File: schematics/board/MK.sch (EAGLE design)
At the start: 19 parts

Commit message: ifdhv
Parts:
- added C2, C3, C4, C5: 100nF, rcl:C-EUC0603
- added R0, R11, R12, R13, R14, R15, R16, R17, R18, R19, R22, R23, R24, R25, R7, R8: 5k1, rcl:R-US_R0603
- added R20: (no value), rcl:R-US_R2512
- added R21: (no value), rcl:R-US_0207/15
- added U$0, U$10, U$11, U$12, U$5, U$7, U$8, U$9: VT93N1, KNPN-2023:VT93N1
- added U$13, U$15: 74HC595, CanCubeSat:74HC595
- added U$14: AD5593, UNKNOWN-2024:AD5593
- added U$16: INA219AID, CanCubeSat:INA219AID
- added U$17: IRF7905PBF, UNKNOWN-2024:IRF7905PBF
- added U$18, U$19, U$20: MOLEX-2-1.25, UNKNOWN-2024:MOLEX-2-1.25
- added U$3: BOARD_SHAPE, UNKNOWN-2024:BOARD_SHAPE
- added X1, X2: JST-2-2.5, UNKNOWN-2024:JST-2-2.5
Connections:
- new net BUS+: X1.1, X2.1
- new net FOTO0: U$20.2
- new net INA_SP+: R19.1, R20.1, R21.1
- new net LATCH: U$13.STCP, U$15.STCP
- new net MOSI: U$13.DS
- new net MOTOR1+: U$13.Q4, U$18.1
- new net MOTOR1-: U$13.Q5, U$18.2
- new net MOTOR2+: U$13.Q2, U$19.1
- new net MOTOR2-: U$13.Q3, U$19.2
- new net N$10: R14.2, U$11.1, U$14.IO6
- new net N$11: C2.1, U$14.VREF
- new net N$12: R15.2, U$12.1, U$14.IO7
- new net N$15: C5.2, R19.2, U$16.A0
- new net N$16: C3.1, C4.1, U$14.VDD, U$14.VDDL
- new net N$17: R16.1, U$14.AO
- new net N$18: C5.1, R18.2, U$16.A1
- new net N$19: R17.1, U$14.RESET
- new net N$20: U$17.D2, X1.2
- new net N$21: U$17.D1, X2.2
- new net N$22: R22.1, R23.2, U$17.G2
- new net N$23: R24.1, R25.2, U$17.G1
- new net N$35: U$13.Q7S, U$15.DS
- new net N$4: R0.2, U$0.1, U$14.IO0
- new net N$5: R8.2, U$14.IO2, U$7.1
- new net N$6: R7.2, U$14.IO1, U$5.1
- new net N$7: R11.2, U$14.IO3, U$8.1
- new net N$8: R12.2, U$14.IO4, U$9.1
- new net N$9: R13.2, U$10.1, U$14.IO5
- new net PERE1: R23.1, U$13.Q6
- new net PERE2: R25.1, U$13.Q7
- new net SCK: U$13.SHCP, U$15.SHCP
- new net SHIFT3: U$15.Q7S
- new net SP+: R18.1, R20.2
- new net SP-: R21.2
- net 3V3: now also R0.1, R11.1, R12.1, R13.1, R14.1, R15.1, R17.2, R7.1, R8.1, U$13.MR, U$13.VCC, U$15.MR, U$15.VCC, U$16.SCL
- net BUZZER: now also U$13.Q1
- net GND: now also C2.2, C3.2, C4.2, R16.2, R22.2, R24.2, U$0.2, U$10.2, U$11.2, U$12.2, U$13.GND, U$13.OE, U$14.GND, U$15.GND, U$15.OE, U$16.IN+, U$16.IN-, U$16.SDA, U$17.S1, U$17.S2, U$20.1, U$5.2, U$7.2, U$8.2, U$9.2
- net SCL: now also U$14.SCL, U$16.VS
- net SDA: now also U$14.SDA, U$16.GND

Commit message: пам пам тидам
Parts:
- added R26, R27, R28, R29, R30, R31, R32, R33, R34, R35, R36, R37: 5k1, rcl:R-US_R0603
- added U$21: MOSFET_2P+2N_AP9930GM, UNKNOWN-2024:MOSFET_2P+2N_AP9930GM
- added U$22, U$23: NDC7002N, UNKNOWN-2024:NDC7002N
- U$15: value 74HC595 -> MOSFET_2P+2N_AP9930GM; device CanCubeSat:74HC595 -> UNKNOWN-2024:MOSFET_2P+2N_AP9930GM
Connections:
- removed net SHIFT3: U$15.Q7S
- new net MK_MOTOR1+: R37.1
- new net MK_MOTOR1-: R36.1
- new net MK_MOTOR2+: R31.1
- new net MK_MOTOR2-: R30.1
- new net N$24: R32.2, R34.1, U$21.N1G, U$21.P1G, U$23.D1
- new net N$25: R26.2, R28.1, U$15.N1G, U$15.P1G, U$22.D1
- new net N$26: R27.2, R29.1, U$15.N2G, U$15.P2G, U$22.D2
- new net N$27: R33.2, R35.1, U$21.N2G, U$21.P2G, U$23.D2
- new net N$28: R34.2, R36.2, U$23.G1
- new net N$29: R35.2, R37.2, U$23.G2
- new net N$32: R28.2, R30.2, U$22.G1
- new net SHIFT2: U$13.Q7S
- net 3V3: no longer U$15.MR, U$15.VCC
- net 5V: now also R26.1, R27.1, R32.1, R33.1, U$15.P1P2S, U$21.P1P2S
- net GND: now also U$15.N1N2S, U$21.N1N2S, U$22.S1, U$22.S2, U$23.S1, U$23.S2; no longer U$15.GND, U$15.OE
- net LATCH: no longer U$15.STCP
- net MOTOR1+: now also U$21.P2N2D
- net MOTOR1-: now also U$21.P1N1D
- net MOTOR2+: now also U$15.P2N2D
- net MOTOR2-: now also U$15.P1N1D
- net N$35: now also R29.2, R31.2, U$22.G2; no longer U$13.Q7S, U$15.DS
- net SCK: no longer U$15.SHCP

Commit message: Платки там
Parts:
- removed R15: 5k1, rcl:R-US_R0603
- removed U$10, U$11, U$12, U$5, U$7, U$8, U$9: VT93N1, KNPN-2023:VT93N1
- added JP1: (no value), pinhead:PINHD-1X10
- added JP2: (no value), pinhead:PINHD-1X16
- added R39, R40, R41, R42, R43, R44, R45, R46: 5k1, rcl:R-US_R0603
- R20: value (none) -> R05
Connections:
- net SD_CK renamed CK_SD
- removed net N$10: R14.2, U$11.1, U$14.IO6
- removed net N$12: R15.2, U$12.1, U$14.IO7
- removed net N$5: R8.2, U$14.IO2, U$7.1
- new net CO: R8.2, U$14.IO2
- new net CS_LIS: STM.PA10
- new net CS_LSM: STM.PA9
- new net H3: R12.2, U$14.IO4
- new net M0_RADIO: STM.PB1
- new net M1_RADIO: STM.PB10
- new net MICS: R13.2, U$14.IO5
- new net MISO_SENS: STM.PB4
- new net MOSI_SENS: STM.PB5
- new net N$34: R13.1, R45.2
- new net N$36: R12.1, R43.2
- new net N$37: R11.1, R41.2
- new net NO2: R11.2, U$14.IO3
- new net RX_GPS: STM.PA3
- new net RX_LIDAR: STM.PA12
- new net RX_RADIO: STM.PB3
- new net SCK_SENS: STM.PA5
- new net TX_GPS: STM.PA2
- new net TX_LIDAR: STM.PA11
- new net TX_RADIO: STM.PA15
- net 3V3: now also R40.1, R42.1, R44.1, R46.1; no longer R11.1, R12.1, R13.1, R14.1, R15.1, R8.1
- net 5V: now also R39.2, R8.1
- net ADC_FOTO: no longer STM.PA0
- net CE_RADIO: no longer STM.PC13
- net CS_RADIO: no longer STM.PC14
- net DIR_DRIVER: no longer STM.PA10
- net FOTO0: now also R7.2, U$14.IO1
- net GND: now also R14.1; no longer U$10.2, U$11.2, U$12.2, U$13.OE, U$5.2, U$7.2, U$8.2, U$9.2
- net IRQ_RADIO: no longer STM.PC15
- net MISO_RADIO: no longer STM.PA11
- net MISO_SR: no longer STM.PB4
- net MOSI_RADIO: no longer STM.PA1
- net MOSI_SR: no longer STM.PB5
- net N$6: now also R39.1, R40.2; no longer R7.2, U$14.IO1, U$5.1
- net N$7: now also R41.1, R42.2; no longer R11.2, U$14.IO3, U$8.1
- net N$8: now also R43.1, R44.2; no longer R12.2, U$14.IO4, U$9.1
- net N$9: now also R45.1, R46.2; no longer R13.2, U$10.1, U$14.IO5
- net OE_SR: now also R14.2, U$13.OE
- net RX1_BLE: no longer STM.PB3
- net RX2_GPS: no longer STM.PA3
- net SCK_RADIO: no longer STM.PB13
- net SCK_SR: no longer STM.PA5
- net STEP_DRIVER: no longer STM.PA9
- net SW_AMP: no longer STM.PA4
- net TX1_BLE: no longer STM.PA15
- net TX2_GPS: no longer STM.PA2
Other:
- moved on the sheet: BME280, BUZZER, C1, C2, C3, C4, C5, MICRO_SD, R0, R1, R10, R11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

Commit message: ПЛАТЫ, АААААААААААААААААААААААААААА
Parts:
- JP2: device pinhead:PINHD-1X16 -> pinhead:PINHD-1X18
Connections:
- removed net BUS+: X1.1, X2.1
- new net 4V: JP1.10, X1.1, X2.1
- new net AUX_RADIO: JP2.10, STM.PC13
- new net C0: JP2.1
- new net GERMO: JP2.18, U$13.Q0
- new net NH3: JP2.3
- new net OE: JP1.4
- new net SHIFT_2: JP2.17
- net 3V3: now also JP2.6
- net 5V: now also JP2.7
- net BUZZER: no longer STM.PB0
- net CS_LIS: now also JP1.8
- net CS_LSM: now also JP1.9
- net GND: now also JP2.5
- net LATCH: now also JP1.5
- net M0_RADIO: now also JP2.12, STM.PC15; no longer STM.PB1
- net M1_RADIO: now also JP2.11, STM.PC14; no longer STM.PB10
- net MICS: now also JP2.4
- net MISO_SENS: now also JP1.2
- net MOSI_SENS: now also JP1.1
- net NO2: now also JP2.2
- net RX_GPS: now also JP2.14
- net RX_LIDAR: now also JP2.15
- net RX_RADIO: now also JP1.6
- net SCK_SENS: now also JP1.3
- net SCL: now also JP2.9
- net SDA: now also JP2.8
- net TX_GPS: now also JP2.13
- net TX_LIDAR: now also JP2.16
- net TX_RADIO: now also JP1.7
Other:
- moved on the sheet: JP1, U$4, U$6

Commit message: схемы плат
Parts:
- removed R11, R12, R13, R39, R40, R41, R42, R43, R44, R45, R46, R8: 5k1, rcl:R-US_R0603
- R0, R7: value 5k1 -> 2k2
- renumbered STM to STM32F411, U$18 to MOTOR_SP_V, U$19 to MOTOR_SP_G, U$20 to FOTO0, X1 to PERE1, X2 to PERE2
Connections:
- removed net H3: R12.2, U$14.IO4
- removed net N$34: R13.1, R45.2
- removed net N$36: R12.1, R43.2
- removed net N$37: R11.1, R41.2
- removed net N$6: R39.1, R40.2
- removed net N$7: R41.1, R42.2
- removed net N$8: R43.1, R44.2
- removed net N$9: R45.1, R46.2
- net 3V3: no longer R40.1, R42.1, R44.1, R46.1
- net 5V: no longer R39.2, R8.1
- net CO: no longer R8.2
- net MICS: no longer R13.2
- net NH3: now also U$14.IO4
- net NO2: no longer R11.2
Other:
- moved on the sheet: C1, R5, R6

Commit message: подготовлены файлы для зимней сессии
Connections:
- removed net LATCH: JP1.5, U$13.STCP
- removed net OE: JP1.4
- removed net SHIFT2: U$13.Q7S
- removed net SHIFT_2: JP2.17
- new net SHIFT: JP2.17, U$13.Q7S
- net LATCH_SR: now also JP1.5, U$13.STCP
- net OE_SR: now also JP1.4
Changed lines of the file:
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@@
 <sheet>
 <plain>
+<wire x1="-208.28" y1="154.94" x2="327.66" y2="154.94" width="0.1524" layer="90"/>
+<wire x1="327.66" y1="154.94" x2="327.66" y2="-109.22" width="0.1524" layer="90"/>
+<wire x1="327.66" y1="-109.22" x2="-208.28" y2="-109.22" width="0.1524" layer="90"/>
+<wire x1="-208.28" y1="-109.22" x2="-208.28" y2="154.94" width="0.1524" layer="90"/>
 </plain>
 <instances>
@@
 <pinref part="R14" gate="G$1" pin="2"/>
 </segment>
+<segment>
+<wire x1="-160.02" y1="88.9" x2="-193.04" y2="88.9" width="0.1524" layer="91"/>
+<label x="-193.04" y="88.9" size="1.778" layer="95"/>
+<pinref part="JP1" gate="A" pin="4"/>
+</segment>
 </net>
 <net name="LATCH_SR" class="0">
@@
 <label x="-355.6" y="-81.28" size="1.778" layer="95"/>
 <pinref part="U$4" gate="G$1" pin="9"/>
+</segment>
+<segment>
+<wire x1="-160.02" y1="86.36" x2="-193.04" y2="86.36" width="0.1524" layer="91"/>
+<label x="-193.04" y="86.36" size="1.778" layer="95"/>
+<pinref part="JP1" gate="A" pin="5"/>
+</segment>
+<segment>
+<pinref part="U$13" gate="G$1" pin="STCP"/>
+<wire x1="93.98" y1="81.28" x2="104.14" y2="81.28" width="0.1524" layer="91"/>
+<label x="96.52" y="81.28" size="1.778" layer="95"/>
 </segment>
 </net>
@@
 </segment>
 </net>
-<net name="LATCH" class="0">
-<segment>
-<pinref part="U$13" gate="G$1" pin="STCP"/>
-<wire x1="93.98" y1="81.28" x2="104.14" y2="81.28" width="0.1524" layer="91"/>
-<label x="96.52" y="81.28" size="1.778" layer="95"/>
-</segment>
-<segment>
-<wire x1="-160.02" y1="86.36" x2="-193.04" y2="86.36" width="0.1524" layer="91"/>
-<label x="-193.04" y="86.36" size="1.778" layer="95"/>
-<pinref part="JP1" gate="A" pin="5"/>
-</segment>
-</net>
 <net name="MOTOR2+" class="0">
 <segment>
@@
 </segment>
 </net>
-<net name="SHIFT2" class="0">
+<net name="SHIFT" class="0">
 <segment>
 <pinref part="U$13" gate="G$1" pin="Q7S"/>
 <wire x1="93.98" y1="73.66" x2="104.14" y2="73.66" width="0.1524" layer="91"/>
 <label x="96.52" y="73.66" size="1.778" layer="95"/>
+</segment>
+<segment>
+<wire x1="-193.04" y1="17.78" x2="-160.02" y2="17.78" width="0.1524" layer="91"/>
+<label x="-193.04" y="17.78" size="1.778" layer="95"/>
+<pinref part="JP2" gate="A" pin="17"/>
 </segment>
 </net>
@@
 </segment>
 </net>
-<net name="OE" class="0">
-<segment>
-<wire x1="-160.02" y1="88.9" x2="-193.04" y2="88.9" width="0.1524" layer="91"/>
-<label x="-193.04" y="88.9" size="1.778" layer="95"/>
-<pinref part="JP1" gate="A" pin="4"/>
-</segment>
-</net>
 <net name="4V" class="0">
 <segment>
@@
 </segment>
 </net>
-<net name="SHIFT_2" class="0">
-<segment>
-<wire x1="-193.04" y1="17.78" x2="-160.02" y2="17.78" width="0.1524" layer="91"/>
-<label x="-193.04" y="17.78" size="1.778" layer="95"/>
-<pinref part="JP2" gate="A" pin="17"/>
-</segment>
-</net>

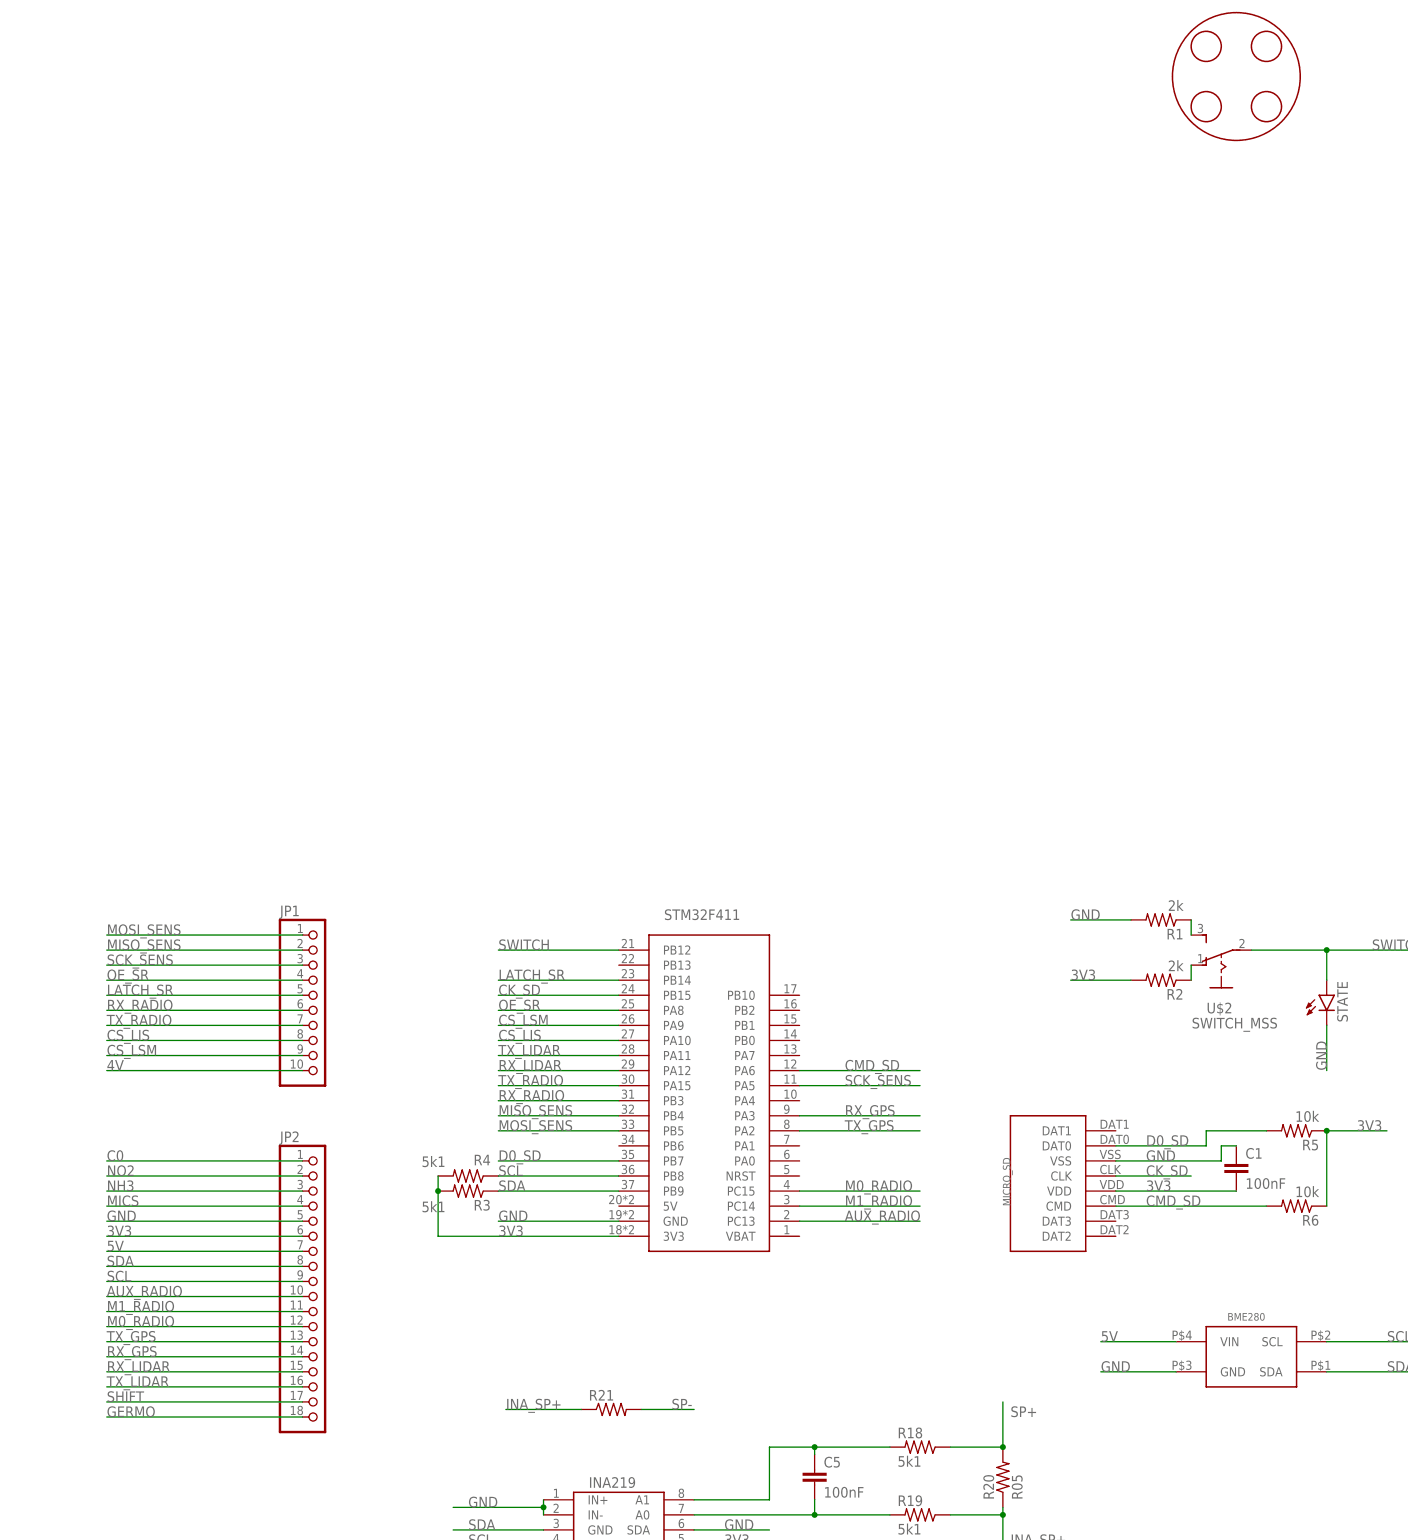
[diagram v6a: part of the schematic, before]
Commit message: распиновка разъемов плат
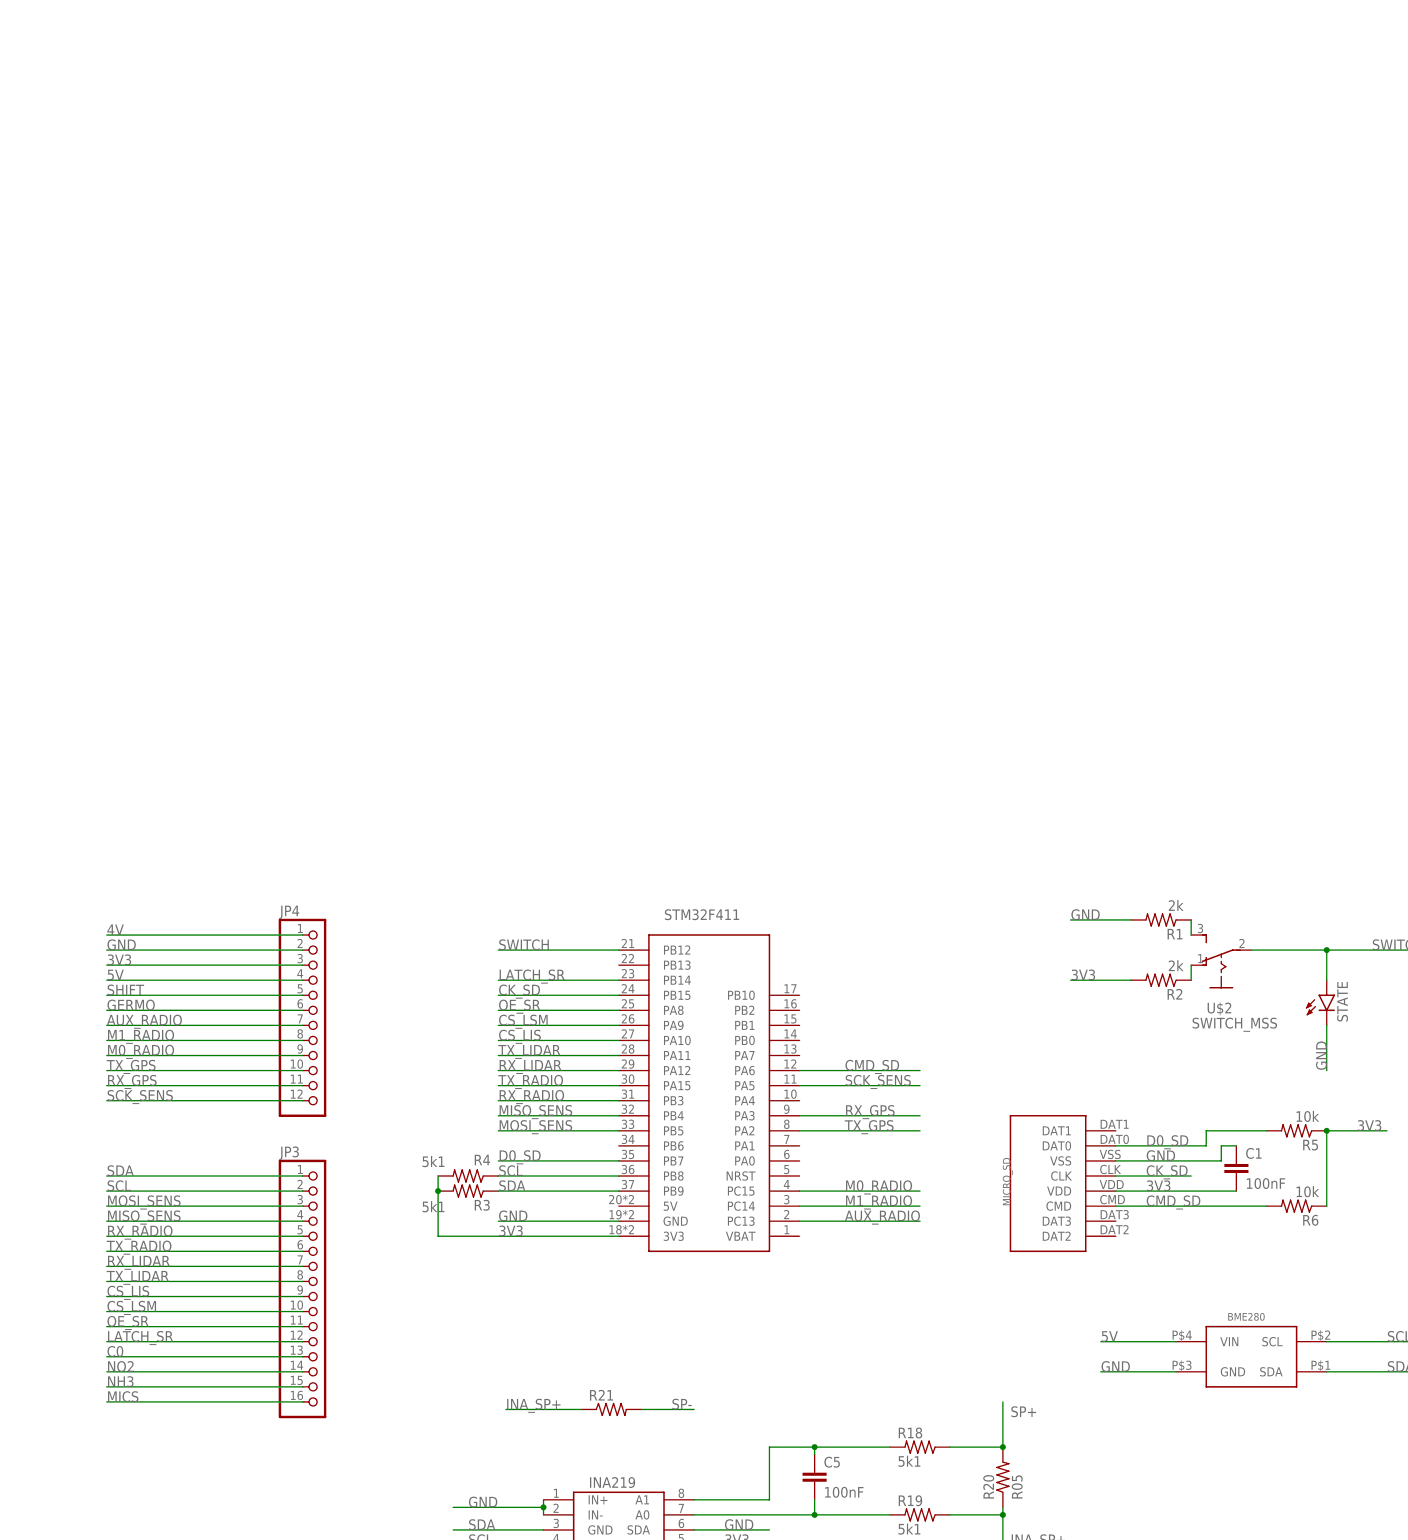
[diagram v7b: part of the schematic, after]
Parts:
- removed JP1: (no value), pinhead:PINHD-1X10
- removed JP2: (no value), pinhead:PINHD-1X18
- removed U$3: BOARD_SHAPE, UNKNOWN-2024:BOARD_SHAPE
- added JP3: (no value), pinhead:PINHD-1X16
- added JP4: (no value), pinhead:PINHD-1X12
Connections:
- net 3V3: now also JP4.3; no longer JP2.6
- net 4V: now also JP4.1; no longer JP1.10
- net 5V: now also JP4.4; no longer JP2.7
- net AUX_RADIO: now also JP4.7; no longer JP2.10
- net C0: now also JP3.13; no longer JP2.1
- net CS_LIS: now also JP3.9; no longer JP1.8
- net CS_LSM: now also JP3.10; no longer JP1.9
- net GERMO: now also JP4.6; no longer JP2.18
- net GND: now also JP4.2; no longer JP2.5
- net LATCH_SR: now also JP3.12; no longer JP1.5
- net M0_RADIO: now also JP4.9; no longer JP2.12
- net M1_RADIO: now also JP4.8; no longer JP2.11
- net MICS: now also JP3.16; no longer JP2.4
- net MISO_SENS: now also JP3.4; no longer JP1.2
- net MOSI_SENS: now also JP3.3; no longer JP1.1
- net NH3: now also JP3.15; no longer JP2.3
- net NO2: now also JP3.14; no longer JP2.2
- net OE_SR: now also JP3.11; no longer JP1.4
- net RX_GPS: now also JP4.11; no longer JP2.14
- net RX_LIDAR: now also JP3.7; no longer JP2.15
- net RX_RADIO: now also JP3.5; no longer JP1.6
- net SCK_SENS: now also JP4.12; no longer JP1.3
- net SCL: now also JP3.2; no longer JP2.9
- net SDA: now also JP3.1; no longer JP2.8
- net SHIFT: now also JP4.5; no longer JP2.17
- net TX_GPS: now also JP4.10; no longer JP2.13
- net TX_LIDAR: now also JP3.8; no longer JP2.16
- net TX_RADIO: now also JP3.6; no longer JP1.7

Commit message: jhgh
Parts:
- removed U$4: PBS_SMD_X13, UNKNOWN-2024:PBS_SMD_X13
- removed U$6: PBS_SMD_X9, UNKNOWN-2024:PBS_SMD_X9
- added SP: MOLEX-2-1.25, UNKNOWN-2024:MOLEX-2-1.25
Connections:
- removed net ADC_FOTO: U$4.4
- removed net CE_RADIO: U$6.9
- removed net CS_RADIO: U$6.8
- removed net DIR_DRIVER: U$4.12
- removed net IRQ_RADIO: U$6.7
- removed net MISO_RADIO: U$6.5
- removed net MISO_SR: U$4.6
- removed net MOSI: U$13.DS
- removed net MOSI_RADIO: U$6.6
- removed net MOSI_SR: U$4.5
- removed net RX1_BLE: U$4.10
- removed net RX2_GPS: U$6.2
- removed net SCK: U$13.SHCP
- removed net SCK_RADIO: U$6.4
- removed net SCK_SR: U$4.7
- removed net STEP_DRIVER: U$4.13
- removed net SW_AMP: U$6.1
- removed net TX1_BLE: U$4.11
- removed net TX2_GPS: U$6.3
- net 3V3: no longer U$4.1
- net 5V: no longer U$4.3
- net GND: no longer U$4.2
- net LATCH_SR: no longer U$4.9
- net MK_MOTOR1+: now also U$13.Q4
- net MK_MOTOR1-: now also U$13.Q5
- net MK_MOTOR2+: now also U$13.Q2
- net MK_MOTOR2-: now also U$13.Q3
- net MOSI_SENS: now also U$13.DS
- net MOTOR1+: no longer U$13.Q4
- net MOTOR1-: no longer U$13.Q5
- net MOTOR2+: no longer U$13.Q2
- net MOTOR2-: no longer U$13.Q3
- net OE_SR: no longer U$4.8
- net SCK_SENS: now also U$13.SHCP
- net SP+: now also SP.1
- net SP-: now also SP.2
